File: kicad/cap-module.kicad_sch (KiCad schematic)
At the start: 2 parts, among them U1 RaspberryPi_Pico, U2 AD7747

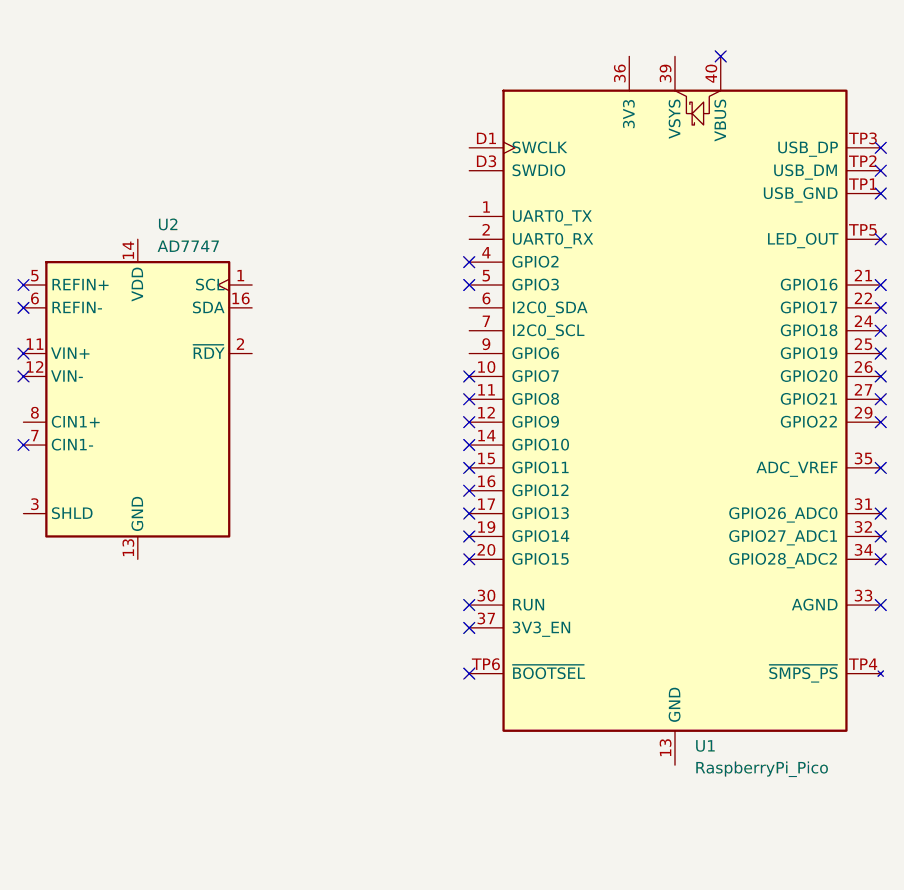
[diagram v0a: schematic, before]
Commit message: Connect data lines
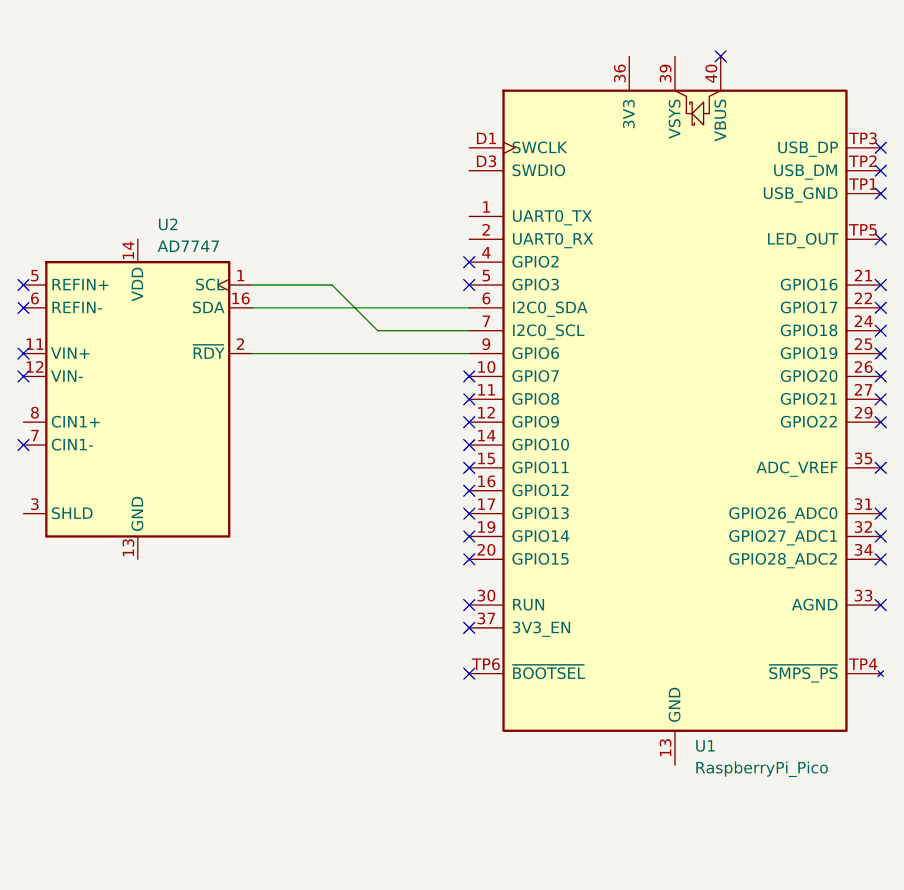
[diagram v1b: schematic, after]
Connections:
- net at U2.1 (SCL): now also U1.7 (GPIO5)
- net at U2.16 (SDA): now also U1.6 (GPIO4)
- net at U2.2 (~{RDY}): now also U1.9 (GPIO6)
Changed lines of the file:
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@@
   (no_connect (at 77.47 92.71))
   (no_connect (at 172.72 90.17))
+  (wire (pts (xy 102.87 92.71) (xy 127 92.71))
+    (stroke (width 0) (type default))
+  )
+  (wire (pts (xy 102.87 87.63) (xy 127 87.63))
+    (stroke (width 0) (type default))
+  )
+  (wire (pts (xy 102.87 85.09) (xy 111.76 85.09))
+    (stroke (width 0) (type default))
+  )
+  (wire (pts (xy 111.76 85.09) (xy 116.84 90.17))
+    (stroke (width 0) (type default))
+  )
+  (wire (pts (xy 116.84 90.17) (xy 127 90.17))
+    (stroke (width 0) (type default))
+  )
   (symbol (lib_id "Analog_ADC_AD7747:AD7747") (at 90.17 97.79 0) (unit 1)
     (in_bom yes) (on_board yes) (dnp no) (fields_autoplaced)

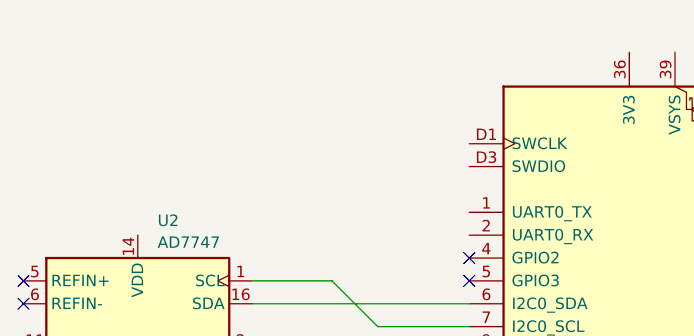
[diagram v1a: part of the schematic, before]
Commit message: Add decoupling capacitors
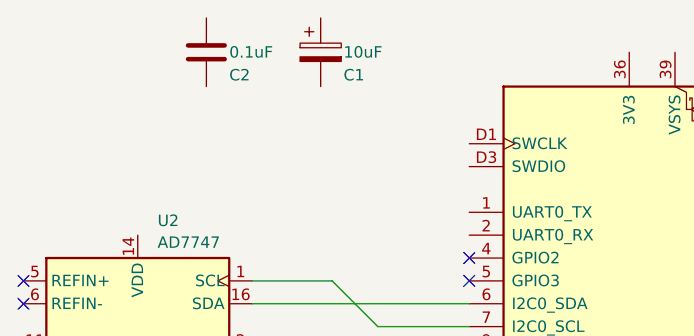
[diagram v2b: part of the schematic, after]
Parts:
- added C1: 10uF, symbol Device:C_Polarized
- added C2: 0.1uF, symbol Device:C
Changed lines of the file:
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@@
     (stroke (width 0) (type default))
+  )
+  (symbol (lib_id "Device:C") (at 97.79 59.69 0) (unit 1)
+    (in_bom yes) (on_board yes) (dnp no)
+    (property "Reference" "C2" (at 100.33 62.23 0)
+      (effects (font (size 1.27 1.27)) (justify left))
+    )
+    (property "Value" "0.1uF" (at 100.33 59.69 0)
+      (effects (font (size 1.27 1.27)) (justify left))
+    )
+    (property "Footprint" "" (at 98.7552 63.5 0)
+      (effects (font (size 1.27 1.27)) hide)
+    )
+    (property "Datasheet" "~" (at 97.79 59.69 0)
+      (effects (font (size 1.27 1.27)) hide)
+    )
+    (pin "1")
+    (pin "2")
+    (instances
+      (project "cap-module"
+        (path "/2da8fa58-ccef-42b1-8320-baeb3fec91e3"
+          (reference "C2") (unit 1)
+        )
+      )
+    )
   )
   (symbol (lib_id "Analog_ADC_AD7747:AD7747") (at 90.17 97.79 0) (unit 1)
@@
         )
       )
+    )
+  )
+  (symbol (lib_id "Device:C_Polarized") (at 110.49 59.69 0) (unit 1)
+    (in_bom yes) (on_board yes) (dnp no)
+    (property "Reference" "C1" (at 113.03 62.23 0)
+      (effects (font (size 1.27 1.27)) (justify left))
+    )
+    (property "Value" "10uF" (at 113.03 59.69 0)
+      (effects (font (size 1.27 1.27)) (justify left))
+    )
+    (property "Footprint" "" (at 111.4552 63.5 0)
+      (effects (font (size 1.27 1.27)) hide)
+    )
+    (property "Datasheet" "~" (at 110.49 59.69 0)
+      (effects (font (size 1.27 1.27)) hide)
+    )
+    (pin "1")
+    (pin "2")
+    (instances
+      (project "cap-module"
+        (path "/2da8fa58-ccef-42b1-8320-baeb3fec91e3"
+          (reference "C1") (unit 1)
+        )
+      )

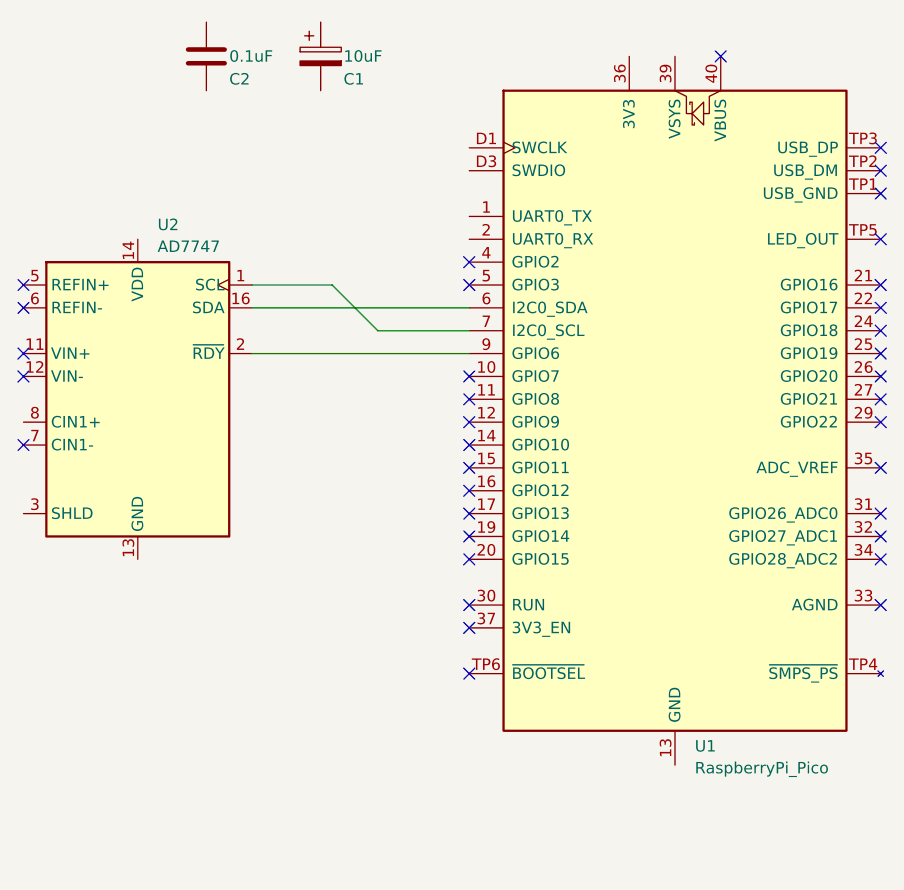
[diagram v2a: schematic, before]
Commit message: Connect power
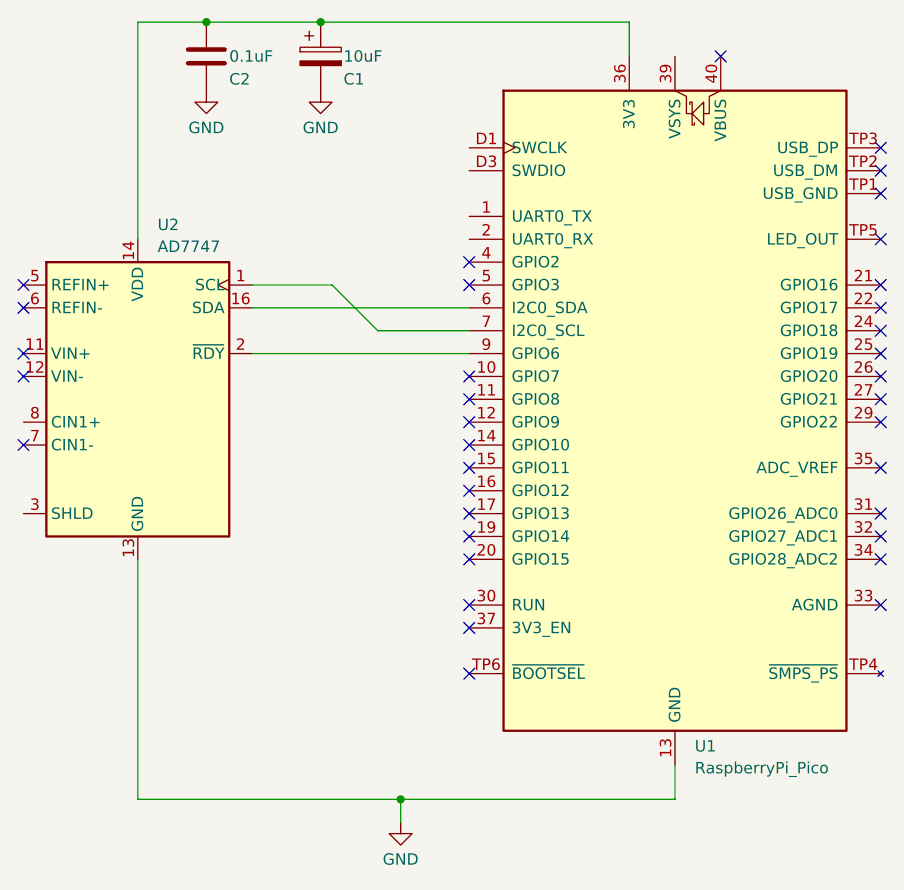
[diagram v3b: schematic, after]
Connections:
- net at C2.1: now also C1.1, U1.36 (3V3), U2.14 (VDD)
- net GND: now reaches C2.2
- net GND: now also C1.2, U1.13 (GND), U1.18 (GND), U1.23 (GND), U1.28 (GND), U1.3 (GND), U1.38 (GND), U1.8 (GND), U1.D2 (GND), U2.13 (GND)
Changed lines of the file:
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@@
 (kicad_sch (version 20230121) (generator eeschema)
   (paper "A4")
+  (junction (at 110.49 55.88) (diameter 0) (color 0 0 0 0)
+  )
+  (junction (at 119.38 142.24) (diameter 0) (color 0 0 0 0)
+  )
+  (junction (at 97.79 55.88) (diameter 0) (color 0 0 0 0)
+  )
   (no_connect (at 172.72 92.71))
   (no_connect (at 77.47 102.87))
@@
     (stroke (width 0) (type default))
   )
+  (wire (pts (xy 90.17 142.24) (xy 119.38 142.24))
+    (stroke (width 0) (type default))
+  )
+  (wire (pts (xy 90.17 55.88) (xy 97.79 55.88))
+    (stroke (width 0) (type default))
+  )
+  (wire (pts (xy 90.17 115.57) (xy 90.17 142.24))
+    (stroke (width 0) (type default))
+  )
+  (wire (pts (xy 144.78 55.88) (xy 144.78 59.69))
+    (stroke (width 0) (type default))
+  )
   (wire (pts (xy 102.87 85.09) (xy 111.76 85.09))
     (stroke (width 0) (type default))
@@
     (stroke (width 0) (type default))
   )
+  (wire (pts (xy 110.49 55.88) (xy 144.78 55.88))
+    (stroke (width 0) (type default))
+  )
+  (wire (pts (xy 97.79 55.88) (xy 110.49 55.88))
+    (stroke (width 0) (type default))
+  )
+  (wire (pts (xy 119.38 144.78) (xy 119.38 142.24))
+    (stroke (width 0) (type default))
+  )
+  (wire (pts (xy 149.86 138.43) (xy 149.86 142.24))
+    (stroke (width 0) (type default))
+  )
+  (wire (pts (xy 90.17 55.88) (xy 90.17 80.01))
+    (stroke (width 0) (type default))
+  )
   (wire (pts (xy 116.84 90.17) (xy 127 90.17))
+    (stroke (width 0) (type default))
+  )
+  (wire (pts (xy 119.38 142.24) (xy 149.86 142.24))
     (stroke (width 0) (type default))
   )
@@
         )
       )
+    )
+  )
+  (symbol (lib_id "power:GND") (at 110.49 63.5 0) (unit 1)
+    (in_bom yes) (on_board yes) (dnp no) (fields_autoplaced)
+    (property "Reference" "#PWR02" (at 110.49 69.85 0)
+      (effects (font (size 1.27 1.27)) hide)
+    )
+    (property "Value" "GND" (at 110.49 67.6331 0)
+      (effects (font (size 1.27 1.27)))
+    )
+    (property "Footprint" "" (at 110.49 63.5 0)
+      (effects (font (size 1.27 1.27)) hide)
+    )
+    (property "Datasheet" "" (at 110.49 63.5 0)
+      (effects (font (size 1.27 1.27)) hide)
+    )
+    (pin "1")
+    (instances
+      (project "cap-module"
+        (path "/2da8fa58-ccef-42b1-8320-baeb3fec91e3"
+          (reference "#PWR02") (unit 1)
+        )
+      )
+    )
+  )
+  (symbol (lib_id "power:GND") (at 97.79 63.5 0) (unit 1)
+    (in_bom yes) (on_board yes) (dnp no) (fields_autoplaced)
+    (property "Reference" "#PWR01" (at 97.79 69.85 0)
+      (effects (font (size 1.27 1.27)) hide)
+    )
+    (property "Value" "GND" (at 97.79 67.6331 0)
+      (effects (font (size 1.27 1.27)))
+    )
+    (property "Footprint" "" (at 97.79 63.5 0)
+      (effects (font (size 1.27 1.27)) hide)
+    )
+    (property "Datasheet" "" (at 97.79 63.5 0)
+      (effects (font (size 1.27 1.27)) hide)
+    )
+    (pin "1")
+    (instances
+      (project "cap-module"
+        (path "/2da8fa58-ccef-42b1-8320-baeb3fec91e3"
+          (reference "#PWR01") (unit 1)
+        )
+      )
+    )
+  )
+  (symbol (lib_id "power:GND") (at 119.38 144.78 0) (unit 1)
+    (in_bom yes) (on_board yes) (dnp no) (fields_autoplaced)
+    (property "Reference" "#PWR03" (at 119.38 151.13 0)
+      (effects (font (size 1.27 1.27)) hide)
+    )
+    (property "Value" "GND" (at 119.38 148.9131 0)
+      (effects (font (size 1.27 1.27)))
+    )
+    (property "Footprint" "" (at 119.38 144.78 0)
+      (effects (font (size 1.27 1.27)) hide)
+    )
+    (property "Datasheet" "" (at 119.38 144.78 0)
+      (effects (font (size 1.27 1.27)) hide)
+    )
+    (pin "1")
+    (instances
+      (project "cap-module"
+        (path "/2da8fa58-ccef-42b1-8320-baeb3fec91e3"
+          (reference "#PWR03") (unit 1)
+        )
+      )
